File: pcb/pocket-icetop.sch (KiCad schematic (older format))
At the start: 32 parts, among them CON1 5V_DC, P1 USB_B, P2 LED_POWER, P3 ICSP, P4 LED_STRIP, SW1 RESET, SW2 SW_DEMO1, SW3 SW_DEMO2, U1 ATMEGA32U4-AU, Y1 Crystal

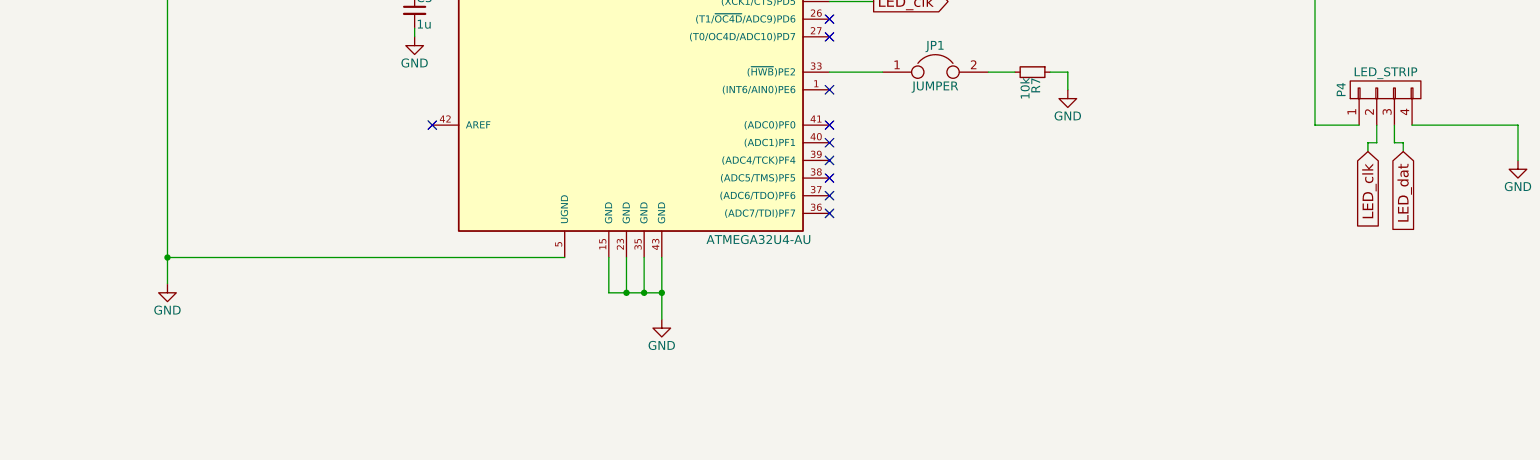
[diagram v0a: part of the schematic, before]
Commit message: Add pull-down on LED_CLK to schematic.
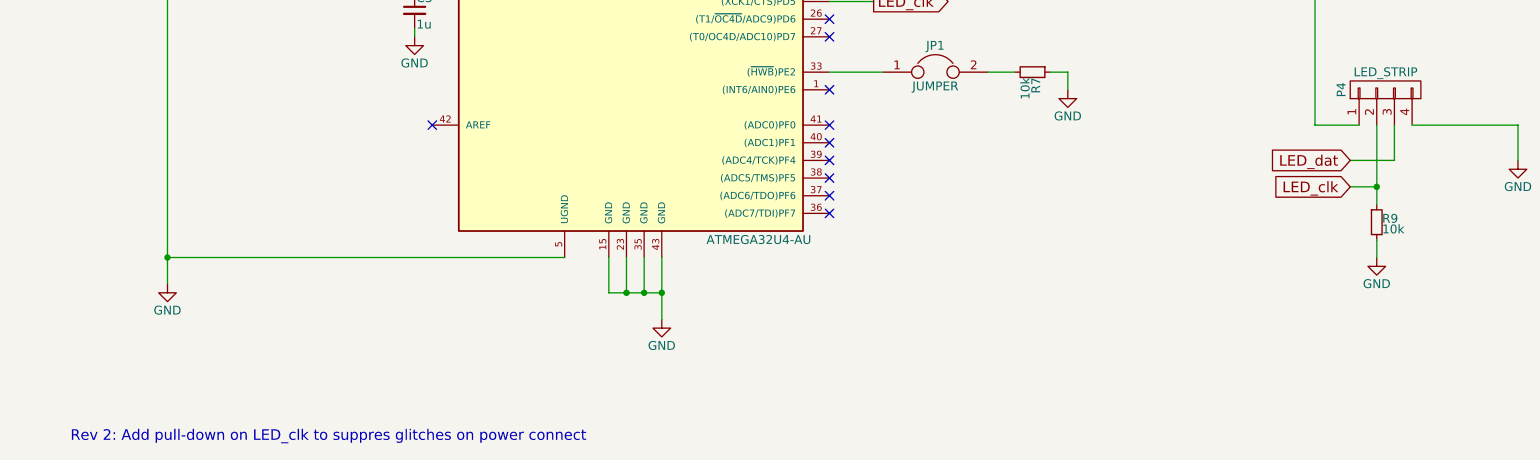
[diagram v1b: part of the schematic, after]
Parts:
- added R9: 10k, symbol R_Small
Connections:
- wire segments 116 -> 115
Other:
- note added: "Rev 2: Add pull-down on LED_clk to suppres glitches on power connect"

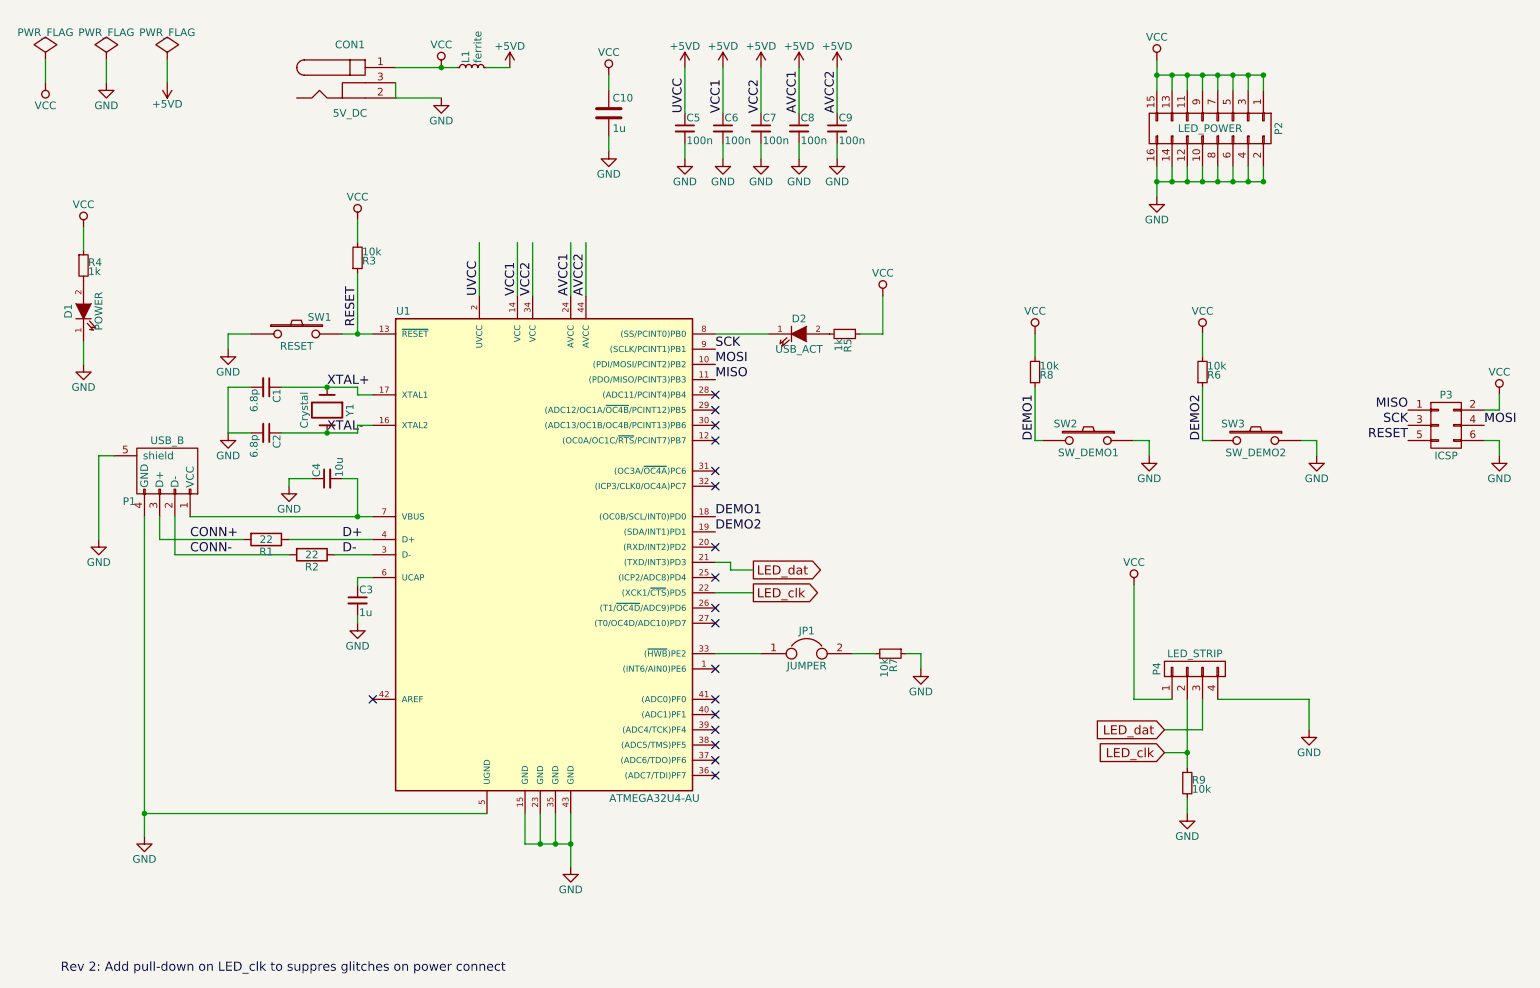
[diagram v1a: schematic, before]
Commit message: Drop DFU jumper by using SW3 as dual-purpose input: demo button and DFU select during reset.
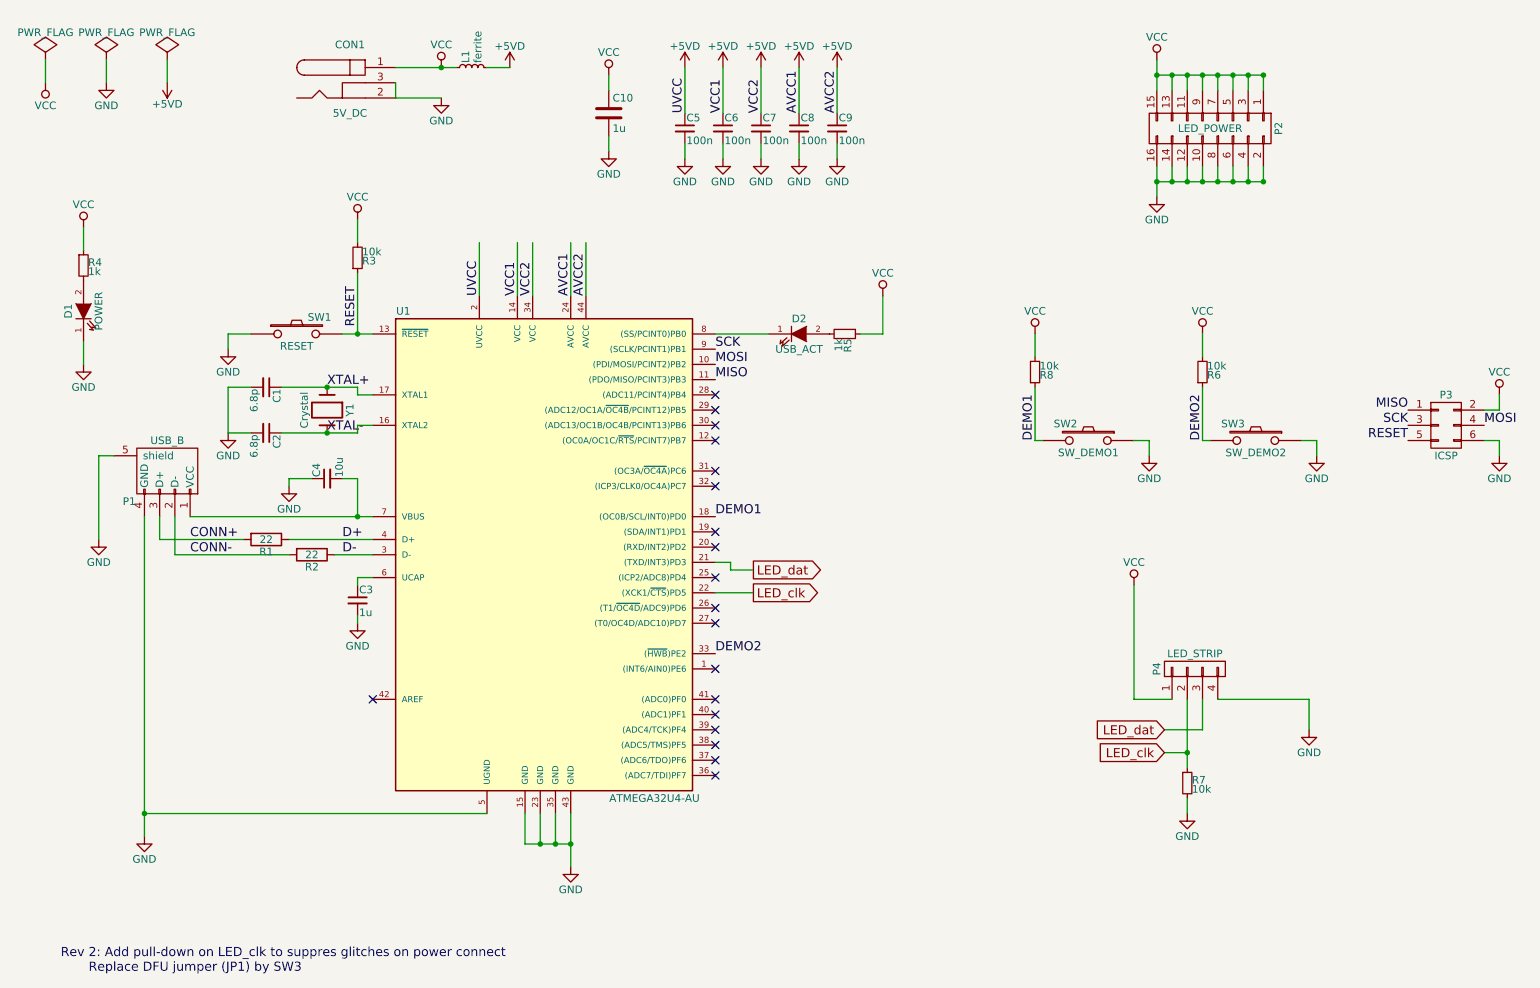
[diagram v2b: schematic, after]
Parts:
- removed JP1: JUMPER, Pin_Headers:Pin_Header_Straight_1x02, symbol JUMPER
- removed R7: 10k, Resistors_SMD:R_0603_HandSoldering, symbol R_Small
- R7: renamed from R9; footprint (none) -> Resistors_SMD:R_0603_HandSoldering; URL (none) -> https://www.conrad.be/ce/nl/product/1375015
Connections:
- wire segments 115 -> 111
- no-connect marks 18 -> 19
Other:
- note added: "Rev 2: Add pull-down on LED_clk to suppres glitches on power connect\n Replace DFU jumper (JP1) by SW3"
- note removed: "Rev 2: Add pull-down on LED_clk to suppres glitches on power connect"
